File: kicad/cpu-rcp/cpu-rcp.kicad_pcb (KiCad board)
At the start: 2 copper layers, 86.4 x 63.5 mm, 96 parts, among them P1 RDRAM-EDGE, P5 NINTENDO-64_PINHEAD-25X2, U1 9480F, U10 CPU-NUS, U7 MX8330, U9 RCP-NUS, X1 14.318MHz

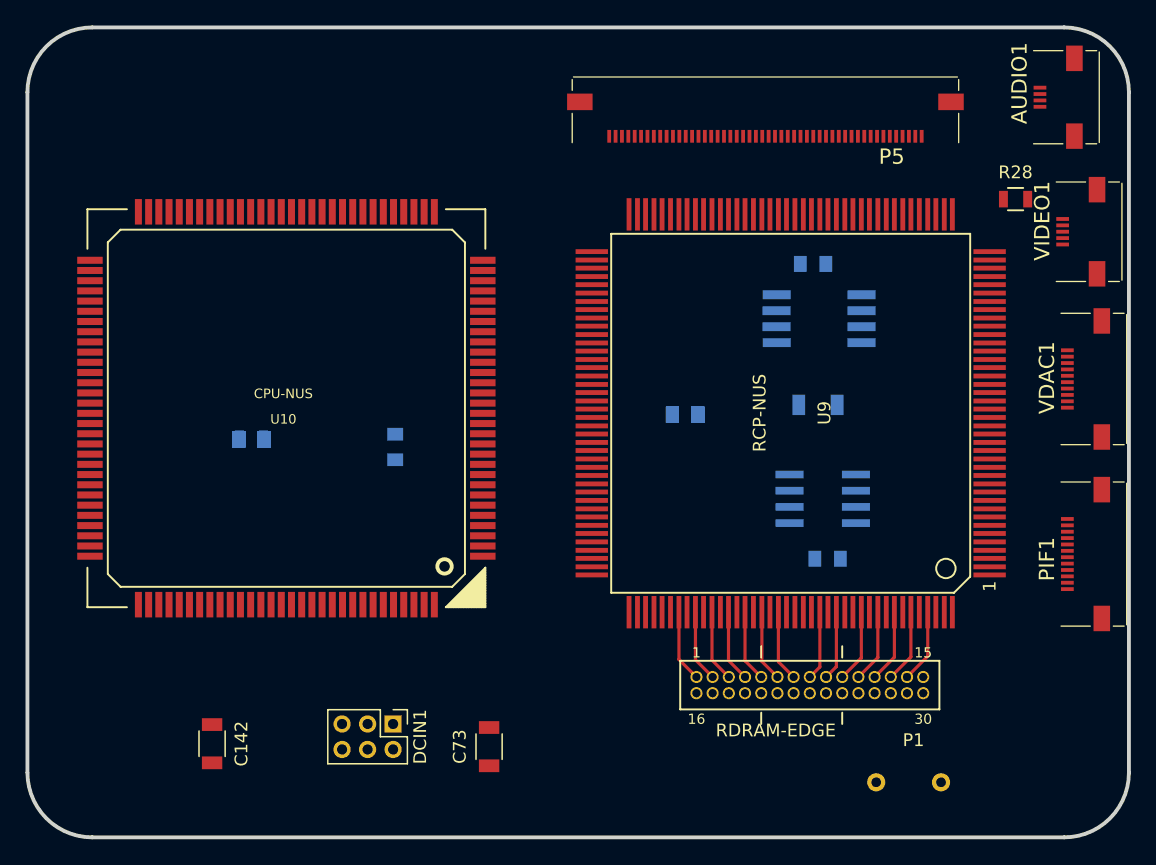
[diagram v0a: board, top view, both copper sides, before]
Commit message: Rebuild to utilize new 3D shapes
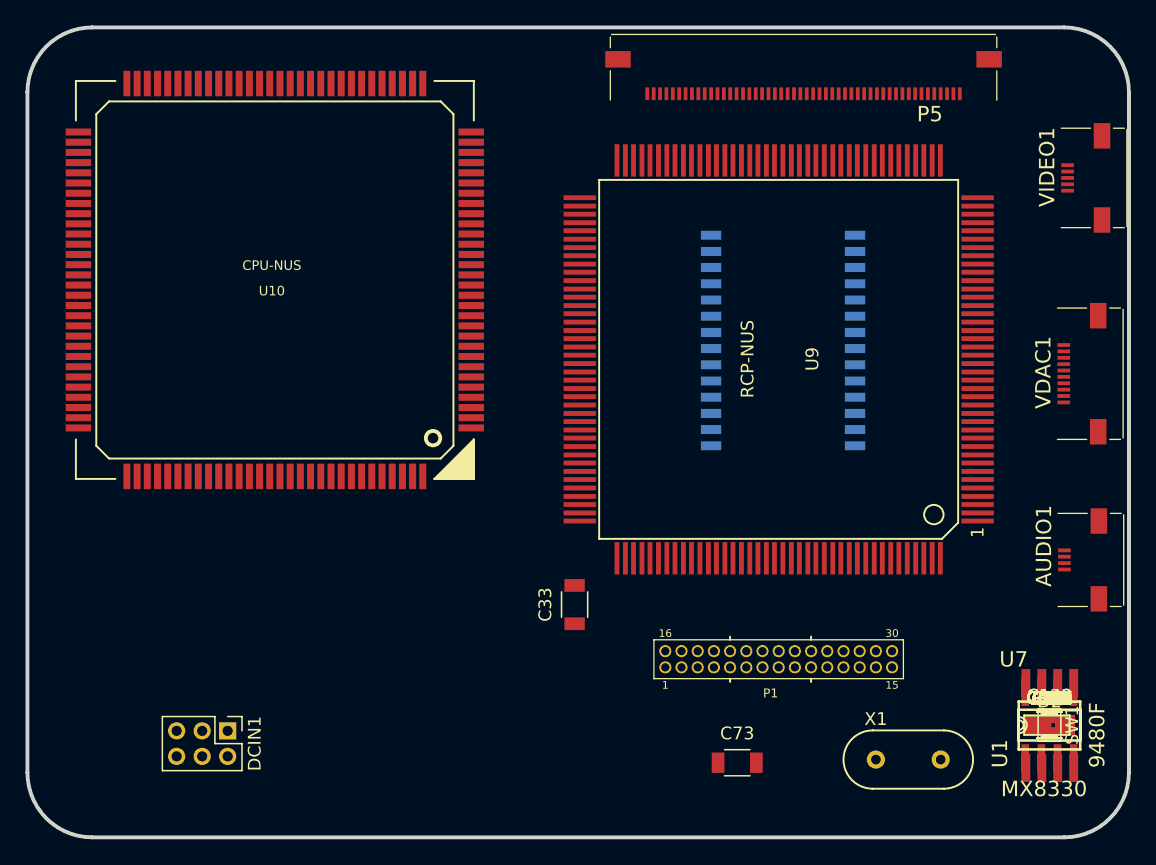
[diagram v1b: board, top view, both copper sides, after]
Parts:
- removed PIF1: PIF I/O, n64:connector-molex-505110-1292
- added C123, C127, C144: ±, Capacitors_SMD:C_0805, F.Cu at (105.5, 80.1)
- added C128: 10uF, Capacitors_SMD:C_1206, F.Cu at (105.5, 80.1)
- added D2: ±, Diodes_SMD:TUMD2, F.Cu at (105.5, 80.1)
- added R2: 2K, Resistors_SMD:R_0805, F.Cu at (105.5, 80.1)
- added R22: 47K, Resistors_SMD:R_0805, F.Cu at (105.5, 80.1)
- added R23: 1K, Resistors_SMD:R_0805, F.Cu at (105.5, 80.1)
- added R3: 30K, Resistors_SMD:R_0805, F.Cu at (105.5, 80.1)
- added R36: 51K, Resistors_SMD:R_0805, F.Cu at (105.5, 80.1)
- added R4: 68K, Resistors_SMD:R_0805, F.Cu at (105.5, 80.1)
- added SW1: Reset, Connectors:GS2, F.Cu at (105.5, 80.1)
- added U6: PIF-NUS, n64:so-28w, B.Cu at (84.6, 50.6)
- C33, C39, C40, C5, C6, C7, C8, C9, CC1, CC10, CC11, CC12, CC13, CC14, CC15, CC16, CC17, CC18, CC19, CC2, CC20, CC21, CC22, CC23, CC24, CC25, CC26, CC27, CC3, CC4, CC5, CC6, CC7, CC8, CC9, CP1, CP2, CP3, CP4, CP5, CP6, CR1, CR10, CR11, CR12, CR13, CR14, CR15, CR16, CR17, CR18, CR19, CR2, CR20, CR21, CR22, CR23, CR24, CR25, CR26, CR27, CR28, CR29, CR3, CR30, CR4, CR5, CR6, CR7, CR8, CR9, CU1, CU7, CV1, CV2, R12, R13, R24, R29, R30, R34, U1, U7, X1: moved to F.Cu
- moved C39 66.5 mm to (105.5, 80.1)
- moved C40 66.5 mm to (105.5, 80.1)
- moved C6 66.5 mm to (105.5, 80.1)
- moved C7 66.5 mm to (105.5, 80.1)
- moved C8 66.5 mm to (105.5, 80.1)
- moved C9 66.5 mm to (105.5, 80.1)
- moved CC1 66.5 mm to (105.5, 80.1)
- moved CC10 66.5 mm to (105.5, 80.1)
- moved CC11 66.5 mm to (105.5, 80.1)
- moved CC12 66.5 mm to (105.5, 80.1)
- moved CC13 66.5 mm to (105.5, 80.1)
- moved CC14 66.5 mm to (105.5, 80.1)
- moved CC15 66.5 mm to (105.5, 80.1)
- moved CC16 66.5 mm to (105.5, 80.1)
- moved CC17 66.5 mm to (105.5, 80.1)
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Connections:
- net /ADDR renamed ADDR
- net /CMD renamed CMD
- net /DQ0 renamed DQ0
- net /DQ1 renamed DQ1
- net /DQ2 renamed DQ2
- net /DQ3 renamed DQ3
- net /DQ4 renamed DQ4
- net /DQ5 renamed DQ5
- net /DQ6 renamed DQ6
- net /DQ7 renamed DQ7
- net /DQ8 renamed DQ8
- net /Peripherals/AUDIO_OUT_L renamed /External connections/AUDIO_OUT_L
- net /Peripherals/AUDIO_OUT_R renamed /External connections/AUDIO_OUT_R
- net /Peripherals/LOUT renamed LOUT
- net /Peripherals/ROUT renamed ROUT
- net /Peripherals/VIDEO_SYNC renamed /External connections/VIDEO_SYNC
- net /RXCLK renamed RXCLK
- net /TXCLK renamed TXCLK
- net /VREF renamed VREF
- DCIN1 pad 4: PGOOD -> ENABLE
- P1 pad 15: PGOOD -> +3V3
- P1 pad 18: GND -> ENABLE
- P1 pad 19: GND -> +3V3
- P1 pad 21: +3V3 -> GND
- P1 pad 22: +3V3 -> GND
- P1 pad 23: GND -> +3V3
- P1 pad 25: +3V3 -> GND
- P1 pad 27: GND -> +3V3
- P1 pad 29: +3V3 -> GND
- P5 pad 13: Net-(P5-Pad13) -> (no net)
- P5 pad 18: /Peripherals/CIC_DATA_OUT -> CIC_IN
- P5 pad 19: /Peripherals/CIC_CLK -> CIC_CLK
- P5 pad 21: /Peripherals/EEPROM_DATA -> EEPROM_DAT
- P5 pad 38: Net-(P5-Pad38) -> (no net)
- P5 pad 43: /Peripherals/CIC_DATA_IN -> CIC_OUT
- U10 pad 18: Net-(U10-Pad18) -> (no net)
- U10 pad 65: Net-(U10-Pad65) -> (no net)
- U10 pad 74: Net-(U10-Pad74) -> (no net)
- U10 pad 95: Net-(U10-Pad95) -> (no net)
- U7 pad 3: Net-(U7-Pad3) -> (no net)
- U7 pad 7: PGOOD -> Net-(C144-Pad1)
- VDAC1 pad 1: GND -> VCLK
- VDAC1 pad 10: VCLK -> GND
- VDAC1 pad 2: SRGB0 -> /DSYNC
- VDAC1 pad 3: SRGB1 -> SRGB6
- VDAC1 pad 4: SRGB2 -> SRGB5
- VDAC1 pad 5: SRGB3 -> SRGB4
- VDAC1 pad 6: SRGB4 -> SRGB3
- VDAC1 pad 7: SRGB5 -> SRGB2
- VDAC1 pad 8: SRGB6 -> SRGB1
- VDAC1 pad 9: /DSYNC -> SRGB0
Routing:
- net DQ8: track 5.75 -> 0.00 mm
- net DQ7: track 5.73 -> 0.00 mm
- net ADDR: track 5.72 -> 0.00 mm
- net DQ6: track 5.71 -> 0.00 mm
- net DQ5: track 5.70 -> 0.00 mm
- net DQ0: track 5.65 -> 0.00 mm
- net DQ1: track 5.64 -> 0.00 mm
- net DQ2: track 5.63 -> 0.00 mm
- net DQ3: track 5.62 -> 0.00 mm
- net VREF: track 5.61 -> 0.00 mm
- net CMD: track 5.59 -> 0.00 mm
- net DQ4: track 5.57 -> 0.00 mm
- net RXCLK: track 5.42 -> 0.00 mm
- net TXCLK: track 5.41 -> 0.00 mm

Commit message: Playing around
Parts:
- P1: footprint n64:rdram-edge -> n64:rdram-edge-smt
- U1: moved to B.Cu
- moved U1 19.6 mm to (104.8, 60.5), turned to 270 degrees
- moved P1 4.59 mm to (75.9, 71.0), turned to 0 degrees
- moved SW1 3.95 mm to (105.5, 76.2)
- moved D2 3.37 mm to (105.4, 76.7)
- moved R22 3.13 mm to (105.2, 77.0)
- moved R24 3.13 mm to (105.2, 77.0)
- moved R28 3.13 mm to (105.2, 77.0)
- moved R23 3.13 mm to (105.2, 77.0)
- moved R4 3.13 mm to (105.2, 77.0)
- moved R29 3.13 mm to (105.2, 77.0)
- moved R13 3.13 mm to (105.2, 77.0)
- moved R12 3.13 mm to (105.3, 77.0)
- moved R30 3.13 mm to (105.3, 77.0)
- moved CR19 3.13 mm to (105.3, 77.0)
- moved CR8 3.13 mm to (105.3, 77.0)
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
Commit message: Laying around, WIP
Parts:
- added REF**: MountingHole_3.2mm_M3, Mounting_Holes:MountingHole_3.2mm_M3_DIN965, F.Cu at (29.0, 29.0)
- C127, C128, C142, CC2, CC4, R22, R23, SW1: moved to B.Cu
- moved R29 111.7 mm to (205.7, 28.3)
- moved R30 108.4 mm to (202.1, 28.3)
- moved R24 105.4 mm to (201.7, 34.6)
- moved C8 104.8 mm to (198.2, 28.3)
- moved R34 102.0 mm to (198.0, 34.6)
- moved C7 100.8 mm to (193.7, 28.3)
- moved C9 98.4 mm to (194.2, 34.6)
- moved C5 96.9 mm to (189.2, 28.3)
- moved C6 94.3 mm to (189.7, 34.6)
- moved CR28 88.6 mm to (179.6, 28.3)
- moved CV2 85.5 mm to (179.6, 34.6)
- moved CR25 84.4 mm to (174.6, 28.3)
- moved CU7 81.1 mm to (174.6, 34.6)
- moved CR10 80.4 mm to (169.6, 28.3)
- moved CR26 76.8 mm to (169.6, 34.6)
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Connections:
- P5 pad 13: (no net) -> Net-(P5-Pad13)
- P5 pad 38: (no net) -> Net-(P5-Pad38)
- U10 pad 18: (no net) -> Net-(U10-Pad18)
- U10 pad 65: (no net) -> Net-(U10-Pad65)
- U10 pad 74: (no net) -> Net-(U10-Pad74)
- U10 pad 95: (no net) -> Net-(U10-Pad95)
- U6 pad 15: (no net) -> Net-(U6-Pad15)
- U6 pad 16: (no net) -> Net-(U6-Pad16)
- U6 pad 17: (no net) -> Net-(U6-Pad17)
- U6 pad 18: (no net) -> Net-(U6-Pad18)
- U6 pad 19: (no net) -> Net-(U6-Pad19)
- U6 pad 20: (no net) -> Net-(U6-Pad20)
- U6 pad 21: (no net) -> Net-(U6-Pad21)
- U6 pad 22: (no net) -> Net-(U6-Pad22)
- U6 pad 26: (no net) -> Net-(U6-Pad26)
- U7 pad 3: (no net) -> Net-(U7-Pad3)

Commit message: Laying out
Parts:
- C123, C144, C39, C40, R12, R13, R3, R4: moved to B.Cu
- CC1, CC10, CC11, CC12, CC13, CC14, CC15, CC16, CC17, CC18, CC19, CC20, CC21, CC22, CC23, CC24, CC25, CC26, CC27, CC3, CC5, CC6, CC7, CC8, CC9, CP1, CP2, CP3, CP4, CP6, CR19, CU1, CV1, CV2: footprint Capacitors_SMD:C_0805 -> Capacitors_SMD:C_0603; moved to B.Cu
- CC2, CC4, CP5, CR1, CR10, CR11, CR12, CR13, CR14, CR15, CR16, CR17, CR18, CR2, CR20, CR21, CR22, CR23, CR24, CR25, CR26, CR27, CR28, CR29, CR3, CR30, CR4, CR5, CR6, CR7, CR8, CR9, CU7: footprint Capacitors_SMD:C_0805 -> Capacitors_SMD:C_0603
- moved R29 149.2 mm to (62.8, 71.3)
- moved R34 149.2 mm to (55.1, 77.6)
- moved C6 149.2 mm to (46.8, 77.6)
- moved C9 149.2 mm to (51.3, 77.6)
- moved R24 149.2 mm to (58.8, 77.6)
- moved R30 139.7 mm to (63.7, 47.4), turned to 180 degrees
- moved C8 138.3 mm to (63.5, 59.4)
- moved C7 132.3 mm to (64.3, 55.9), turned to 90 degrees
- moved R2 131.8 mm to (34.8, 73.7)
- moved C5 127.4 mm to (64.0, 52.0), turned to 90 degrees
- moved CV2 96.6 mm to (93.2, 77.7)
- moved CC11 95.3 mm to (40.8, 45.7)
- moved CC19 95.3 mm to (45.8, 45.7)
- moved CC20 95.3 mm to (50.8, 45.7)
- moved CC9 95.3 mm to (35.8, 45.7)
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
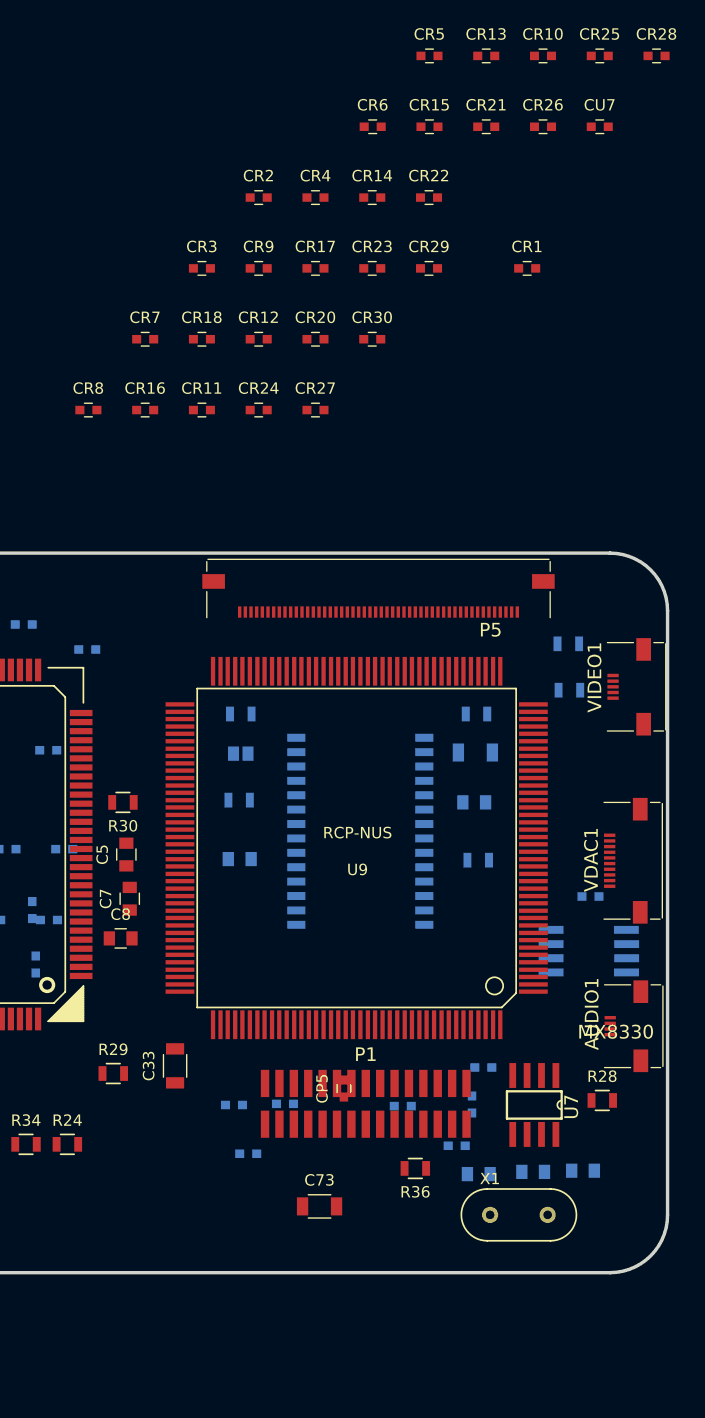
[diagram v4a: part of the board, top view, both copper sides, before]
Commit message: Cleanups for less decoupler capacitors
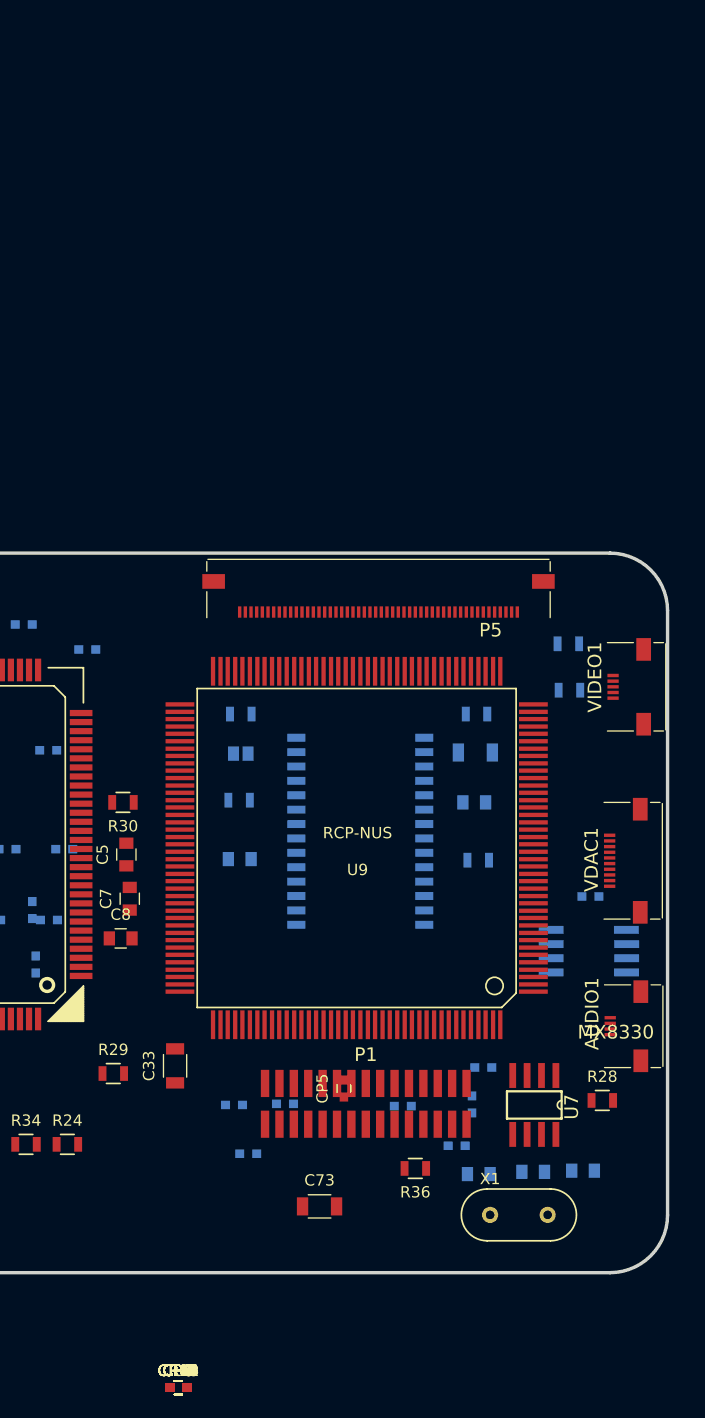
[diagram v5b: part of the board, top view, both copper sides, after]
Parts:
- removed CR16, CR17, CR18, CR20, CR21, CR22, CR23, CR24, CR25, CR26, CR27, CR28, CR29, CR30: 100nF, Capacitors_SMD:C_0603
- moved CR10 121.9 mm to (68.6, 99.1)
- moved CR13 120.6 mm to (68.6, 99.1)
- moved CR5 119.6 mm to (68.6, 99.1)
- moved CU7 117.3 mm to (68.6, 99.1)
- moved CR15 113.5 mm to (68.6, 99.1)
- moved CR6 112.6 mm to (68.6, 99.1)
- moved CR14 106.4 mm to (68.6, 99.1)
- moved CR4 105.7 mm to (68.6, 99.1)
- moved CR2 105.3 mm to (68.6, 99.1)
- moved CR1 103.5 mm to (68.6, 99.1)
- moved CR9 99.0 mm to (68.6, 99.1)
- moved CR3 98.8 mm to (68.6, 99.1)
- moved CR12 92.8 mm to (68.6, 99.1)
- moved CR7 92.6 mm to (68.6, 99.1)
- moved CR8 86.6 mm to (68.6, 99.1)
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
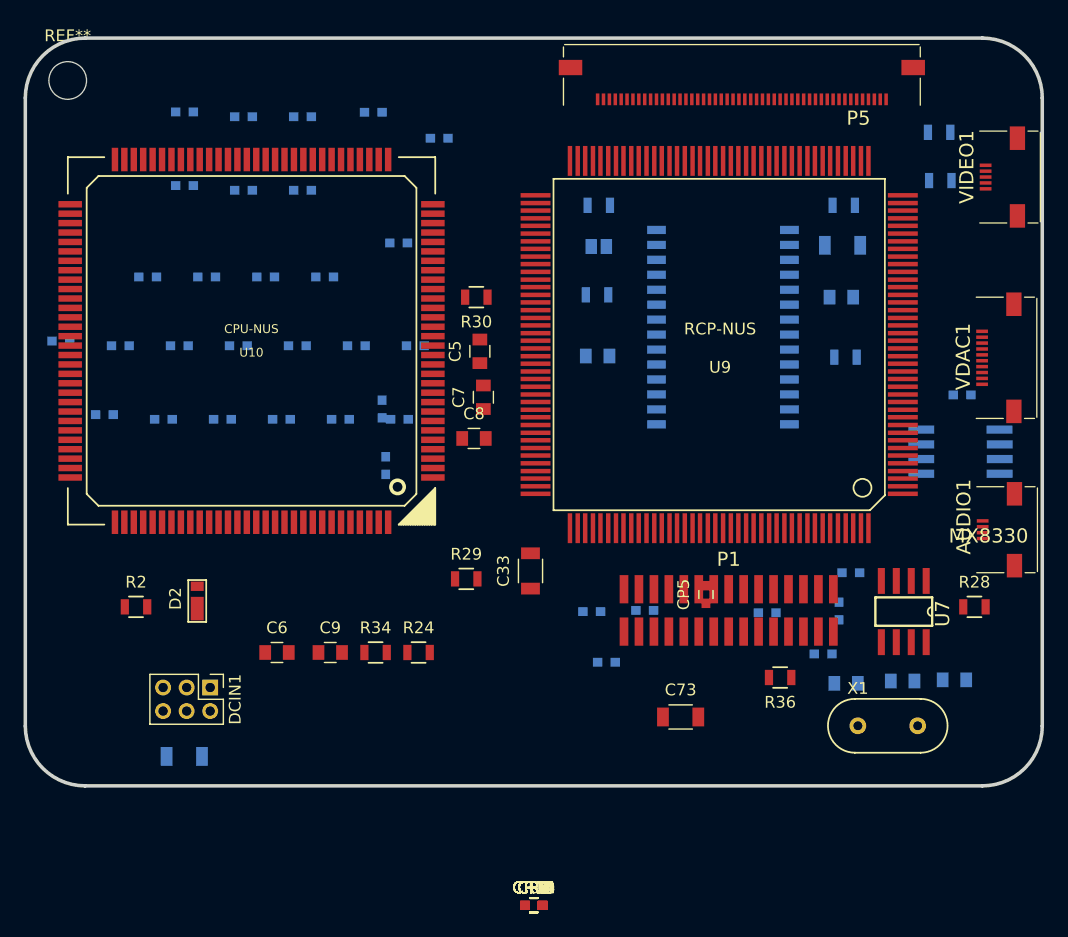
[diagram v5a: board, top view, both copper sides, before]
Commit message: Adjusted to local 3D shape copies for consistent 3D view
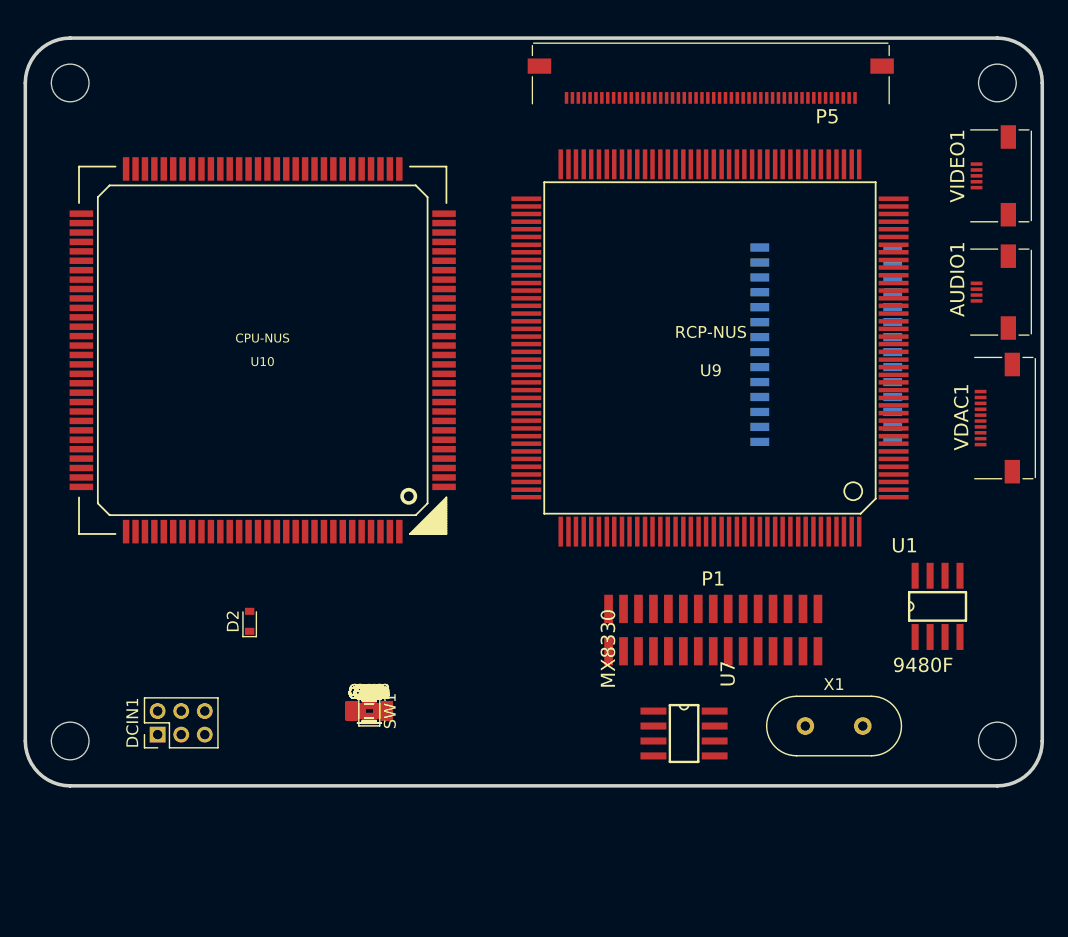
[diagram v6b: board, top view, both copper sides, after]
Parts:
- removed CC10, CC11, CC12, CC13, CC14, CC15, CC16, CC17, CC18, CC19, CC20, CC21, CC22, CC23, CC24, CC25, CC26, CC27, CR19: 100nF, Capacitors_SMD:C_0603
- added REF**: MountingHole_3.2mm_M3, Mounting_Holes:MountingHole_3.2mm_M3_DIN965, F.Cu at (108.0, 29.2)
- added REF**: MountingHole_3.2mm_M3, Mounting_Holes:MountingHole_3.2mm_M3_DIN965, F.Cu at (108.0, 85.1)
- added REF**: MountingHole_3.2mm_M3, Mounting_Holes:MountingHole_3.2mm_M3_DIN965, F.Cu at (29.2, 85.1)
- C123, C127, C128, C142, C144, C39, C40, CC1, CC2, CC3, CC4, CC5, CC6, CC7, CC8, CC9, CP1, CP2, CP3, CP4, CP6, CU1, CV1, CV2, R12, R13, R22, R23, R3, R4, SW1, U1: moved to F.Cu
- D2: footprint Diodes_SMD:TUMD2 -> Diodes_SMD:D_0603
- U7: footprint n64:so-08 -> n64:so-8
- X1: footprint Crystals:HC-49V -> n64:Crystal_HC49-4H_Vertical
- moved R12 69.0 mm to (54.6, 82.5)
- moved R13 66.2 mm to (54.6, 82.5)
- moved R3 58.9 mm to (54.6, 82.5)
- moved CU1 57.0 mm to (54.6, 82.5)
- moved C128 56.4 mm to (54.6, 82.5)
- moved C127 53.3 mm to (54.6, 82.5)
- moved R28 52.1 mm to (54.6, 82.5)
- moved R4 50.4 mm to (54.6, 82.5)
- moved C40 49.8 mm to (54.6, 82.5)
- moved CC6 47.3 mm to (54.6, 82.5)
- moved R22 47.2 mm to (54.6, 82.5)
- moved C144 45.4 mm to (54.6, 82.5)
- moved SW1 44.0 mm to (54.6, 82.5), turned to 0 degrees
- moved CV1 42.5 mm to (54.6, 82.5)
- moved CC9 41.4 mm to (54.6, 82.5)
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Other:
- outline, holes or cut-outs redrawn

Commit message: Work in progress
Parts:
- C123, C127, C144, C39, C40, C5, C6, C7, C8, C9: footprint Capacitors_SMD:C_0805 -> n64:C_0805
- C128, C142, C33, C73: footprint Capacitors_SMD:C_1206 -> n64:CP_Tantalum_Case-D_EIA-7343-31_Reflow
- CC1, CC2, CC3, CC4, CC5, CC6, CC7, CC8, CC9, CP1, CP2, CP3, CP4, CP5, CP6, CR1, CR10, CR11, CR12, CR13, CR14, CR15, CR2, CR3, CR4, CR5, CR6, CR7, CR8, CR9, CU1, CU7, CV1, CV2: footprint Capacitors_SMD:C_0603 -> n64:C_0603
- D2: footprint Diodes_SMD:D_0603 -> n64:D_TUMD2
- R12, R13, R2, R22, R23, R28, R3, R34, R36, R4: footprint Resistors_SMD:R_0805 -> n64:R_0603
- R24, R29, R30: footprint Resistors_SMD:R_0805 -> n64:R_0805
- SW1: footprint Connectors:GS2 -> n64:Connectors_GS2
- X1: footprint n64:Crystal_HC49-4H_Vertical -> n64:Crystal_HC-49V
